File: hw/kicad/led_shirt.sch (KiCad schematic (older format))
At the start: 26 parts, among them J1 10103593-0001LF, J2 2_PIN_HDR, J3 2_PIN_HDR, J4 5_PIN_HDR, Q1 PN_MOSFET_DUAL, SW1 SW_PUSH, U1 AP3012, U2 PIC12F1822, U3 MCP73831

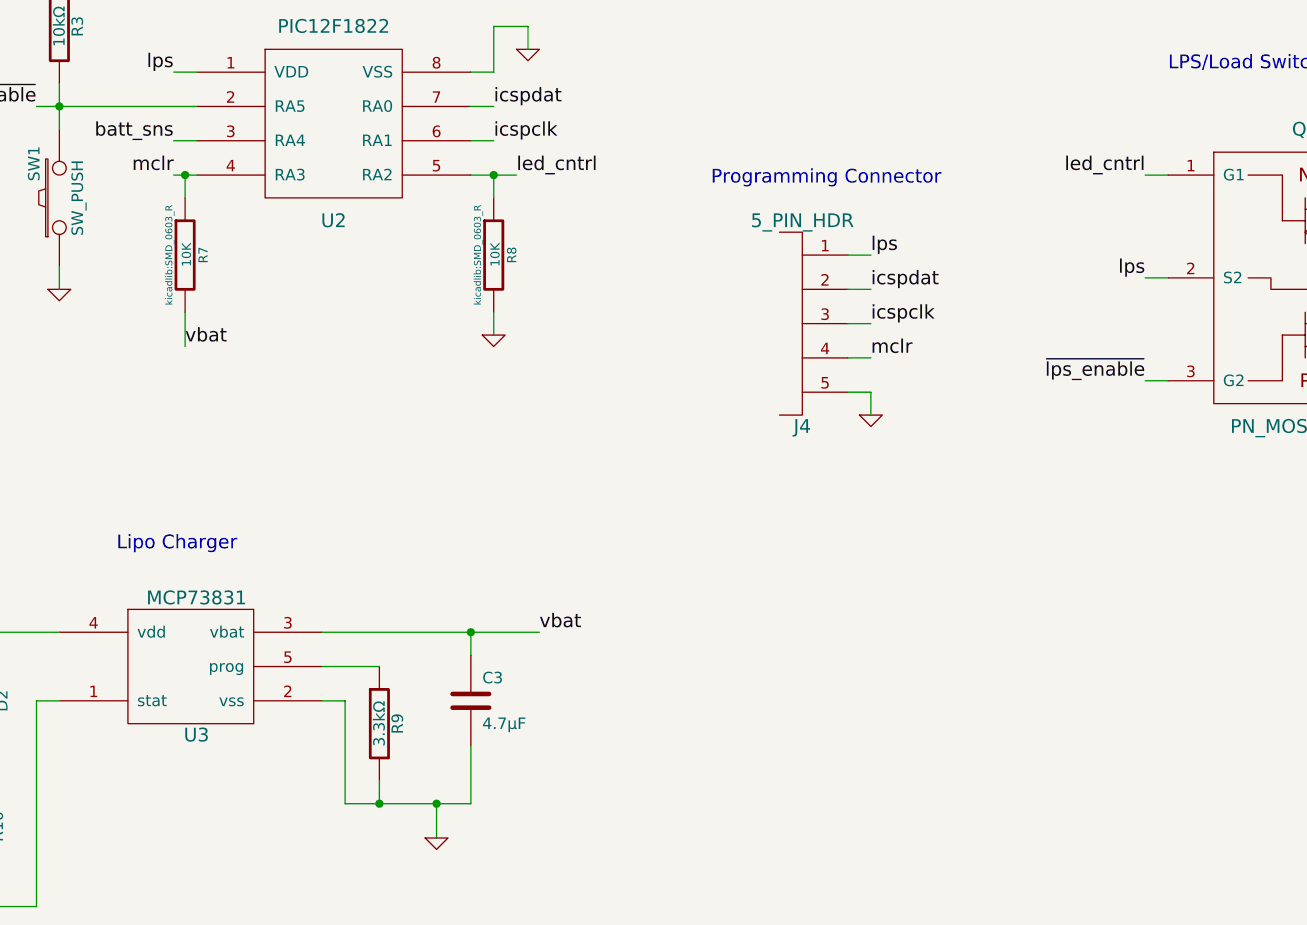
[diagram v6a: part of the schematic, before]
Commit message: add add pull-down to lps net, to prevent p-fet leakage from enabling 12v boost when lps is disabled
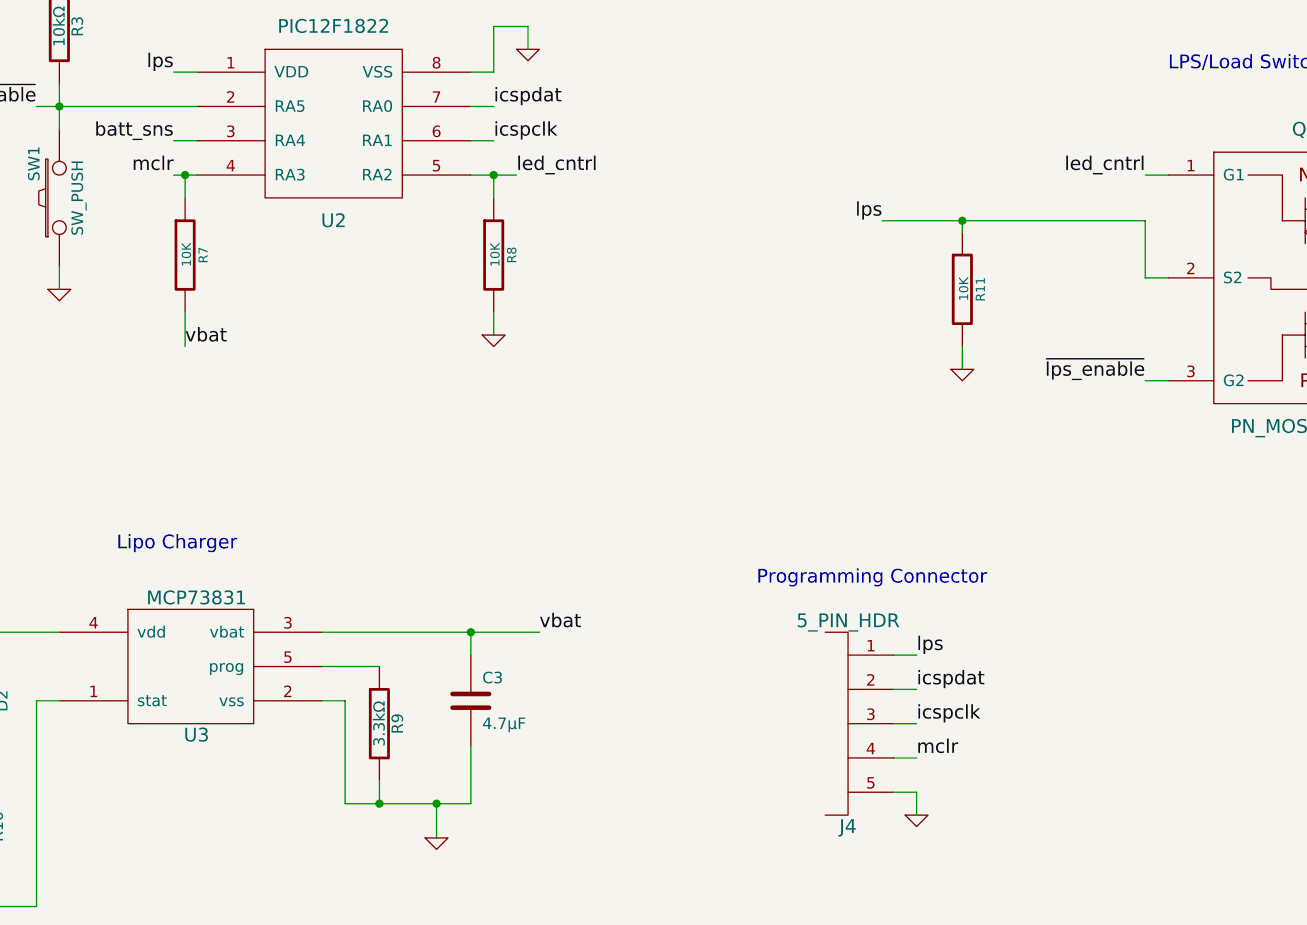
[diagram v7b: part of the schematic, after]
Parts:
- added R11: 10K, kicadlib:SMD_0603_R, symbol R-RESCUE-led_shirt
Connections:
- net GND: now also R11.2
- net lps: now also R11.1
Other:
- moved on the sheet: J4
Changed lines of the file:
@@
 encoding utf-8
 Sheet 1 1
-Title ""
-Date "8 nov 2013"
-Rev ""
+Title "Ledshirt Schematic"
+Date "2015-12-18"
+Rev "v3.1"
 Comp ""
 Comment1 ""
@@
 F 0 "R3" V 2130 3500 50  0000 C CNN
 F 1 "10kΩ" V 2050 3500 50  0000 C CNN
-F 2 "kicadlib:SMD_0603_R" H 2050 3500 60  0001 C CNN
+F 2 "kicadlib:SMD_0603_R" H 2000 3500 28  0001 C CNN
 F 3 "" H 2050 3500 60  0001 C CNN
 	1    2050 3500
@@
 vbat
 $Comp
-L GND-RESCUE-led_shirt #PWR01
+L GND-RESCUE-led_shirt #PWR5
 U 1 1 509D02E2
 P 4100 3600
-F 0 "#PWR01" H 4100 3600 30  0001 C CNN
+F 0 "#PWR5" H 4100 3600 30  0001 C CNN
 F 1 "GND" H 4100 3530 30  0001 C CNN
 F 2 "" H 4100 3600 60  0001 C CNN
@@
 vbat
 $Comp
-L GND-RESCUE-led_shirt #PWR02
+L GND-RESCUE-led_shirt #PWR12
 U 1 1 509D029F
 P 3700 7050
-F 0 "#PWR02" H 3700 7050 30  0001 C CNN
+F 0 "#PWR12" H 3700 7050 30  0001 C CNN
 F 1 "GND" H 3700 6980 30  0001 C CNN
 F 2 "" H 3700 7050 60  0001 C CNN
@@
 $EndComp
 $Comp
-L GND-RESCUE-led_shirt #PWR03
+L GND-RESCUE-led_shirt #PWR10
 U 1 1 509D017A
 P 1250 6750
-F 0 "#PWR03" H 1250 6750 30  0001 C CNN
+F 0 "#PWR10" H 1250 6750 30  0001 C CNN
 F 1 "GND" H 1250 6680 30  0001 C CNN
 F 2 "" H 1250 6750 60  0001 C CNN
@@
 vbus
 $Comp
-L GND-RESCUE-led_shirt #PWR04
+L GND-RESCUE-led_shirt #PWR2
 U 1 1 509D0101
 P 1450 1700
-F 0 "#PWR04" H 1450 1700 30  0001 C CNN
+F 0 "#PWR2" H 1450 1700 30  0001 C CNN
 F 1 "GND" H 1450 1630 30  0001 C CNN
 F 2 "" H 1450 1700 60  0001 C CNN
@@
 F 0 "R7" V 2680 4500 40  0000 C CNN
 F 1 "10K" V 2607 4501 40  0000 C CNN
-F 2 "kicadlib:SMD_0603_R" V 2530 4500 30  0000 C CNN
+F 2 "kicadlib:SMD_0603_R" H 2530 4500 30  0001 C CNN
 F 3 "~" H 2600 4500 30  0000 C CNN
 	1    2600 4500
@@
 F 0 "R8" V 4030 4500 40  0000 C CNN
 F 1 "10K" V 3957 4501 40  0000 C CNN
-F 2 "kicadlib:SMD_0603_R" V 3880 4500 30  0000 C CNN
+F 2 "kicadlib:SMD_0603_R" H 3880 4500 30  0001 C CNN
 F 3 "~" H 3950 4500 30  0000 C CNN
 	1    3950 4500
@@
 $EndComp
 $Comp
-L GND-RESCUE-led_shirt #PWR05
+L GND-RESCUE-led_shirt #PWR7
 U 1 1 56338053
 P 2050 4650
-F 0 "#PWR05" H 2050 4650 30  0001 C CNN
+F 0 "#PWR7" H 2050 4650 30  0001 C CNN
 F 1 "GND" H 2050 4580 30  0001 C CNN
 F 2 "" H 2050 4650 60  0001 C CNN
@@
 Text Label 6800 5050 2    60   ~ 0
 ~lps_enable
-Text Label 6800 4600 2    60   ~ 0
+Text Label 5650 4350 2    60   ~ 0
 lps
 $Comp
-L GND-RESCUE-led_shirt #PWR06
+L GND-RESCUE-led_shirt #PWR8
 U 1 1 5638CC8A
 P 8300 4700
-F 0 "#PWR06" H 8300 4700 30  0001 C CNN
+F 0 "#PWR8" H 8300 4700 30  0001 C CNN
 F 1 "GND" H 8300 4630 30  0001 C CNN
 F 2 "" H 8300 4700 60  0000 C CNN
@@
 $EndComp
 $Comp
-L GND-RESCUE-led_shirt #PWR07
+L GND-RESCUE-led_shirt #PWR9
 U 1 1 5638D6FF
 P 3950 4850
-F 0 "#PWR07" H 3950 4850 30  0001 C CNN
+F 0 "#PWR9" H 3950 4850 30  0001 C CNN
 F 1 "GND" H 3950 4780 30  0001 C CNN
 F 2 "" H 3950 4850 60  0000 C CNN
@@
 L 5_PIN_HDR J4
 U 1 1 56421892
-P 5300 4800
-F 0 "J4" H 5300 4350 60  0000 C CNN
-F 1 "5_PIN_HDR" H 5300 5250 60  0000 C CNN
-F 2 "kicadlib:SMD_JST_5_PIN_VERT" H 5300 4800 60  0001 C CNN
-F 3 "" H 5300 4800 60  0000 C CNN
-	1    5300 4800
-	1    0    0    -1
-$EndComp
-Text Label 5600 4500 0    60   ~ 0
+P 5500 6550
+F 0 "J4" H 5500 6100 60  0000 C CNN
+F 1 "5_PIN_HDR" H 5500 7000 60  0000 C CNN
+F 2 "kicadlib:SMD_JST_5_PIN_VERT" H 5500 6550 60  0001 C CNN
+F 3 "" H 5500 6550 60  0000 C CNN
+	1    5500 6550
+	1    0    0    -1
+$EndComp
+Text Label 5800 6250 0    60   ~ 0
 lps
 $Comp
-L GND-RESCUE-led_shirt #PWR08
+L GND-RESCUE-led_shirt #PWR11
 U 1 1 56421A53
-P 5600 5200
-F 0 "#PWR08" H 5600 5200 30  0001 C CNN
-F 1 "GND" H 5600 5130 30  0001 C CNN
-F 2 "" H 5600 5200 60  0000 C CNN
-F 3 "" H 5600 5200 60  0000 C CNN
-	1    5600 5200
-	1    0    0    -1
-$EndComp
-Text Label 5600 4800 0    60   ~ 0
+P 5800 6950
+F 0 "#PWR11" H 5800 6950 30  0001 C CNN
+F 1 "GND" H 5800 6880 30  0001 C CNN
+F 2 "" H 5800 6950 60  0000 C CNN
+F 3 "" H 5800 6950 60  0000 C CNN
+	1    5800 6950
+	1    0    0    -1
+$EndComp
+Text Label 5800 6550 0    60   ~ 0
 icspclk
-Text Label 5600 4650 0    60   ~ 0
+Text Label 5800 6400 0    60   ~ 0
 icspdat
-Text Label 5600 4950 0    60   ~ 0
+Text Label 5800 6700 0    60   ~ 0
 mclr
 Text Label 2550 4000 2    60   ~ 0
@@
 $EndComp
 $Comp
-L GND-RESCUE-led_shirt #PWR09
+L GND-RESCUE-led_shirt #PWR6
 U 1 1 564229D9
 P 1150 4650
-F 0 "#PWR09" H 1150 4650 30  0001 C CNN
+F 0 "#PWR6" H 1150 4650 30  0001 C CNN
 F 1 "GND" H 1150 4580 30  0001 C CNN
 F 2 "" H 1150 4650 60  0001 C CNN
@@
 $EndComp
 $Comp
-L GND-RESCUE-led_shirt #PWR010
+L GND-RESCUE-led_shirt #PWR3
 U 1 1 56423691
 P 6300 1850
-F 0 "#PWR010" H 6300 1850 30  0001 C CNN
+F 0 "#PWR3" H 6300 1850 30  0001 C CNN
 F 1 "GND" H 6300 1780 30  0001 C CNN
 F 2 "" H 6300 1850 60  0000 C CNN
@@
 $EndComp
 $Comp
-L GND-RESCUE-led_shirt #PWR011
+L GND-RESCUE-led_shirt #PWR1
 U 1 1 56423DAF
 P 2700 1600
-F 0 "#PWR011" H 2700 1600 30  0001 C CNN
+F 0 "#PWR1" H 2700 1600 30  0001 C CNN
 F 1 "GND" H 2700 1530 30  0001 C CNN
 F 2 "" H 2700 1600 60  0000 C CNN
@@
 	1    0    0    -1
 $EndComp
-Text Notes 4900 4200 0    60   ~ 0
+Text Notes 5100 5950 0    60   ~ 0
 Programming Connector
 $Comp
@@
 *LPS output also\nused for 12v enable
 $Comp
-L GND-RESCUE-led_shirt #PWR012
+L GND-RESCUE-led_shirt #PWR4
 U 1 1 564250CE
 P 5550 2700
-F 0 "#PWR012" H 5550 2700 30  0001 C CNN
+F 0 "#PWR4" H 5550 2700 30  0001 C CNN
 F 1 "GND" H 5550 2630 30  0001 C CNN
 F 2 "" H 5550 2700 60  0000 C CNN
@@
 	1    0    0    -1
 $EndComp
+Text Notes 5950 900  0    60   ~ 0
++12v Supply
+Text Label 7400 1650 0    60   ~ 0
+vbat
+Text Label 4650 1200 2    60   ~ 0
++12v
+$Comp
+L 2_PIN_HDR J3
+U 1 1 56426881
+P 9600 3700
+F 0 "J3" H 9600 3550 60  0000 C CNN
+F 1 "2_PIN_HDR" H 9600 4000 60  0000 C CNN
+F 2 "kicadlib:TH_JST_2PIN_RIGHTANGLE" H 9600 3700 60  0001 C CNN
+F 3 "" H 9600 3700 60  0000 C CNN
+	1    9600 3700
+	1    0    0    -1
+$EndComp
+Text Label 8300 3450 0    60   ~ 0
+led-
+Text Label 9900 3550 0    60   ~ 0
++12v
+Text Label 9900 3700 0    60   ~ 0
+led-
+Text Notes 9450 3250 0    60   ~ 0
+LED Output
+Text Notes 6900 3700 0    60   ~ 0
+LPS/Load Switches
+$Comp
+L CP1 C4
+U 1 1 564507C5
+P 5000 1850
+F 0 "C4" H 5025 1950 50  0000 L CNN
+F 1 "CP1" H 5025 1750 50  0000 L CNN
+F 2 "kicadlib:SMD_5X5.2_CAP" H 5000 1850 60  0001 C CNN
+F 3 "" H 5000 1850 60  0000 C CNN
+	1    5000 1850
+	1    0    0    -1
+$EndComp
+Text Notes 4100 1950 0    60   ~ 0
+*nopop-\nextra holdup\non +12V
+Text Notes 5900 2600 0    60   ~ 0
+Vout = 1.25V * (1 + R1/R2)\nUse 82k/10k -> 11.5V, or 10.5V<->12.5V WCA
+$Comp
+L R-RESCUE-led_shirt R11
+U 1 1 5674329D
+P 6000 4650
+F 0 "R11" V 6080 4650 40  0000 C CNN
+F 1 "10K" V 6007 4651 40  0000 C CNN
+F 2 "kicadlib:SMD_0603_R" H 5930 4650 30  0001 C CNN
+F 3 "~" H 6000 4650 30  0000 C CNN
+	1    6000 4650
+	1    0    0    -1
+$EndComp
 Wire Wire Line
 	2550 4150 2650 4150
@@
 Connection ~ 2050 3850
 Wire Wire Line
-	5500 5100 5600 5100
-Wire Wire Line
-	5600 5100 5600 5200
-Wire Wire Line
-	5600 4950 5500 4950
-Wire Wire Line
-	5500 4800 5600 4800
-Wire Wire Line
-	5600 4650 5500 4650
-Wire Wire Line
-	5500 4500 5600 4500
+	5700 6850 5800 6850
+Wire Wire Line
+	5800 6850 5800 6950
+Wire Wire Line
+	5800 6700 5700 6700
+Wire Wire Line
+	5700 6550 5800 6550
+Wire Wire Line
+	5800 6400 5700 6400
+Wire Wire Line
+	5700 6250 5800 6250
 Wire Wire Line
 	2550 4000 2650 4000
@@
 	5350 1650 5350 1200
 Connection ~ 5750 1200
-Text Notes 5950 900  0    60   ~ 0
-+12v Supply
 Connection ~ 7300 1650
 Connection ~ 5350 1200
-Text Label 7400 1650 0    60   ~ 0
-vbat
-Text Label 4650 1200 2    60   ~ 0
-+12v
 Wire Wire Line
 	8300 4050 8300 4150
-$Comp
-L 2_PIN_HDR J3
-U 1 1 56426881
-P 9600 3700
-F 0 "J3" H 9600 3550 60  0000 C CNN
-F 1 "2_PIN_HDR" H 9600 4000 60  0000 C CNN
-F 2 "kicadlib:TH_JST_2PIN_RIGHTANGLE" H 9600 3700 60  0001 C CNN
-F 3 "" H 9600 3700 60  0000 C CNN
-	1    9600 3700
-	1    0    0    -1
-$EndComp
 Wire Wire Line
 	8300 3550 8300 3450
-Text Label 8300 3450 0    60   ~ 0
-led-
-Text Label 9900 3550 0    60   ~ 0
-+12v
-Text Label 9900 3700 0    60   ~ 0
-led-
 Wire Wire Line
 	9900 3550 9800 3550
 Wire Wire Line
 	9800 3700 9900 3700
-Text Notes 9450 3250 0    60   ~ 0
-LED Output
-Text Notes 6900 3700 0    60   ~ 0
-LPS/Load Switches
-$Comp
-L CP1 C4
-U 1 1 564507C5
-P 5000 1850
-F 0 "C4" H 5025 1950 50  0000 L CNN
-F 1 "CP1" H 5025 1750 50  0000 L CNN
-F 2 "kicadlib:SMD_5X5.2_CAP" H 5000 1850 60  0001 C CNN
-F 3 "" H 5000 1850 60  0000 C CNN
-	1    5000 1850
-	1    0    0    -1
-$EndComp
 Wire Wire Line
 	5000 1700 5000 1200
@@
 Wire Notes Line
 	5200 1450 4750 1450
-Text Notes 4100 1950 0    60   ~ 0
-*nopop-\nextra holdup\non +12V
-Text Notes 5900 2600 0    60   ~ 0
-Vout = 1.25V * (1 + R1/R2)\nUse 82k/10k -> 11.5V, or 10.5V<->12.5V WCA
+Wire Wire Line
+	5650 4350 6800 4350
+Wire Wire Line
+	6000 4350 6000 4400
+Wire Wire Line
+	6800 4350 6800 4600
+Connection ~ 6000 4350
+$Comp
+L GND-RESCUE-led_shirt #PWR?
+U 1 1 5674595F
+P 6000 5000
+F 0 "#PWR?" H 6000 5000 30  0001 C CNN
+F 1 "GND" H 6000 4930 30  0001 C CNN
+F 2 "" H 6000 5000 60  0000 C CNN
+F 3 "" H 6000 5000 60  0000 C CNN
+	1    6000 5000
+	1    0    0    -1
+$EndComp
+Wire Wire Line
+	6000 5000 6000 4900
 $EndSCHEMATC
